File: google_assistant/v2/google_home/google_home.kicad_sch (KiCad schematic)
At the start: 22 parts, among them J1 Conn_01x16_MountingPin, J2 AudioJack2_SwitchT, J3 Conn_02x05_Odd_Even, J4 Conn_01x02, SW1 SW_SPDT, SW2 SW_SPDT, U1 R-78E5.0-1.0

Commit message: Fixed FFC connector footprint
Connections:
- net +5V: now also J1.2 (Pin_2), J1.3 (Pin_3), J1.4 (Pin_4), J1.5 (Pin_5), J1.6 (Pin_6), J1.7 (Pin_7); no longer J1.10 (Pin_10), J1.11 (Pin_11), J1.12 (Pin_12), J1.13 (Pin_13), J1.14 (Pin_14), J1.15 (Pin_15)
- net GND: now also J1.11 (Pin_11), J1.12 (Pin_12), J1.13 (Pin_13), J1.14 (Pin_14), J1.15 (Pin_15), J1.8 (Pin_8); no longer J1.2 (Pin_2), J1.3 (Pin_3), J1.4 (Pin_4), J1.5 (Pin_5), J1.6 (Pin_6), J1.9 (Pin_9)
- net at SW1.2 (B): now also J1.16 (Pin_16); no longer J1.1 (Pin_1)
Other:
- moved on the sheet: J1
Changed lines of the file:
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@@
+    (stroke (width 0) (type default))
+  )
+  (wire (pts (xy 190.5 48.26) (xy 195.58 48.26))
     (stroke (width 0) (type default))
   )
@@
     )
   )
-  (symbol (lib_id "power:GND") (at 190.5 96.52 0) (unit 1)
-    (in_bom yes) (on_board yes) (dnp no) (fields_autoplaced)
-    (property "Reference" "#PWR01" (at 190.5 102.87 0)
-      (effects (font (size 1.27 1.27)) hide)
-    )
-    (property "Value" "GND" (at 190.5 101.6 0)
-      (effects (font (size 1.27 1.27)))
-    )
-    (property "Footprint" "" (at 190.5 96.52 0)
-      (effects (font (size 1.27 1.27)) hide)
-    )
-    (property "Datasheet" "" (at 190.5 96.52 0)
+  (symbol (lib_id "power:GND") (at 195.58 48.26 0) (unit 1)
+    (in_bom yes) (on_board yes) (dnp no) (fields_autoplaced)
+    (property "Reference" "#PWR01" (at 195.58 54.61 0)
+      (effects (font (size 1.27 1.27)) hide)
+    )
+    (property "Value" "GND" (at 195.58 53.34 0)
+      (effects (font (size 1.27 1.27)))
+    )
+    (property "Footprint" "" (at 195.58 48.26 0)
+      (effects (font (size 1.27 1.27)) hide)
+    )
+    (property "Datasheet" "" (at 195.58 48.26 0)
       (effects (font (size 1.27 1.27)) hide)
     )
@@
     )
   )
-  (symbol (lib_id "Connector_Generic_MountingPin:Conn_01x16_MountingPin") (at 190.5 71.12 0) (unit 1)
-    (in_bom yes) (on_board yes) (dnp no) (fields_autoplaced)
-    (property "Reference" "J1" (at 193.04 71.4756 0)
+  (symbol (lib_id "Connector_Generic_MountingPin:Conn_01x16_MountingPin") (at 190.5 73.66 0) (mirror x) (unit 1)
+    (in_bom yes) (on_board yes) (dnp no)
+    (property "Reference" "J1" (at 193.04 73.3044 0)
       (effects (font (size 1.27 1.27)) (justify left))
     )
-    (property "Value" "Conn_01x16_MountingPin" (at 193.04 74.0156 0)
+    (property "Value" "Conn_01x16_MountingPin" (at 193.04 70.7644 0)
       (effects (font (size 1.27 1.27)) (justify left))
     )
-    (property "Footprint" "Connector_FFC-FPC:TE_1-1734839-6_1x16-1MP_P0.5mm_Horizontal" (at 190.5 71.12 0)
-      (effects (font (size 1.27 1.27)) hide)
-    )
-    (property "Datasheet" "~" (at 190.5 71.12 0)
-      (effects (font (size 1.27 1.27)) hide)
-    )
+    (property "Footprint" "Connector_FFC-FPC:TE_1-1734839-6_1x16-1MP_P0.5mm_Horizontal" (at 190.5 73.66 0)
+      (effects (font (size 1.27 1.27)) hide)
+    )
+    (property "Datasheet" "~" (at 190.5 73.66 0)
+      (effects (font (size 1.27 1.27)) hide)
+    )

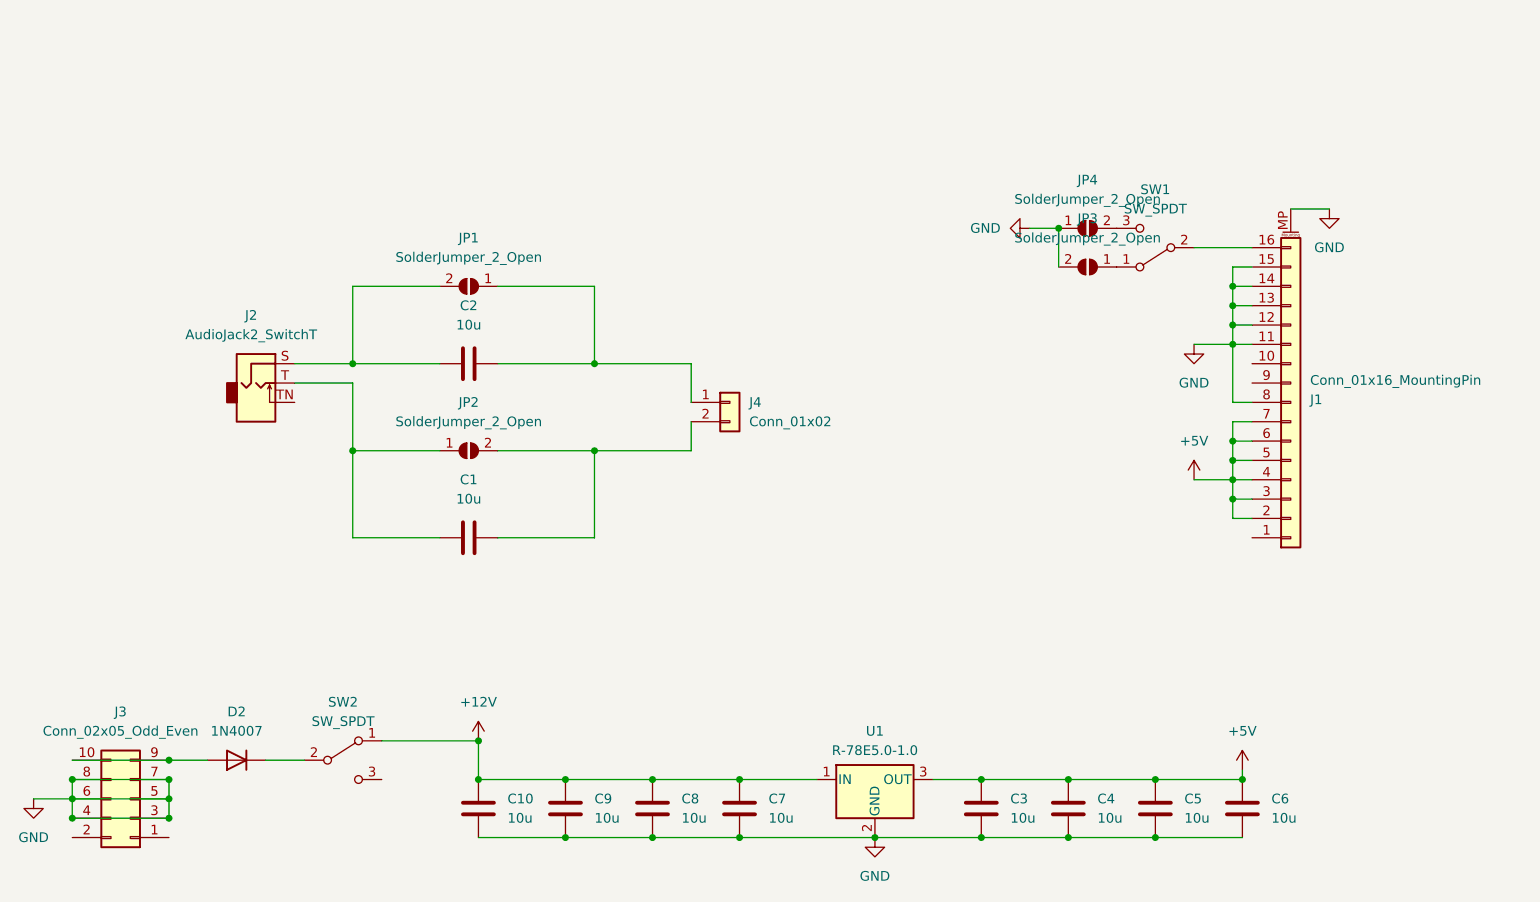
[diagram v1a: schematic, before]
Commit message: Added transformer
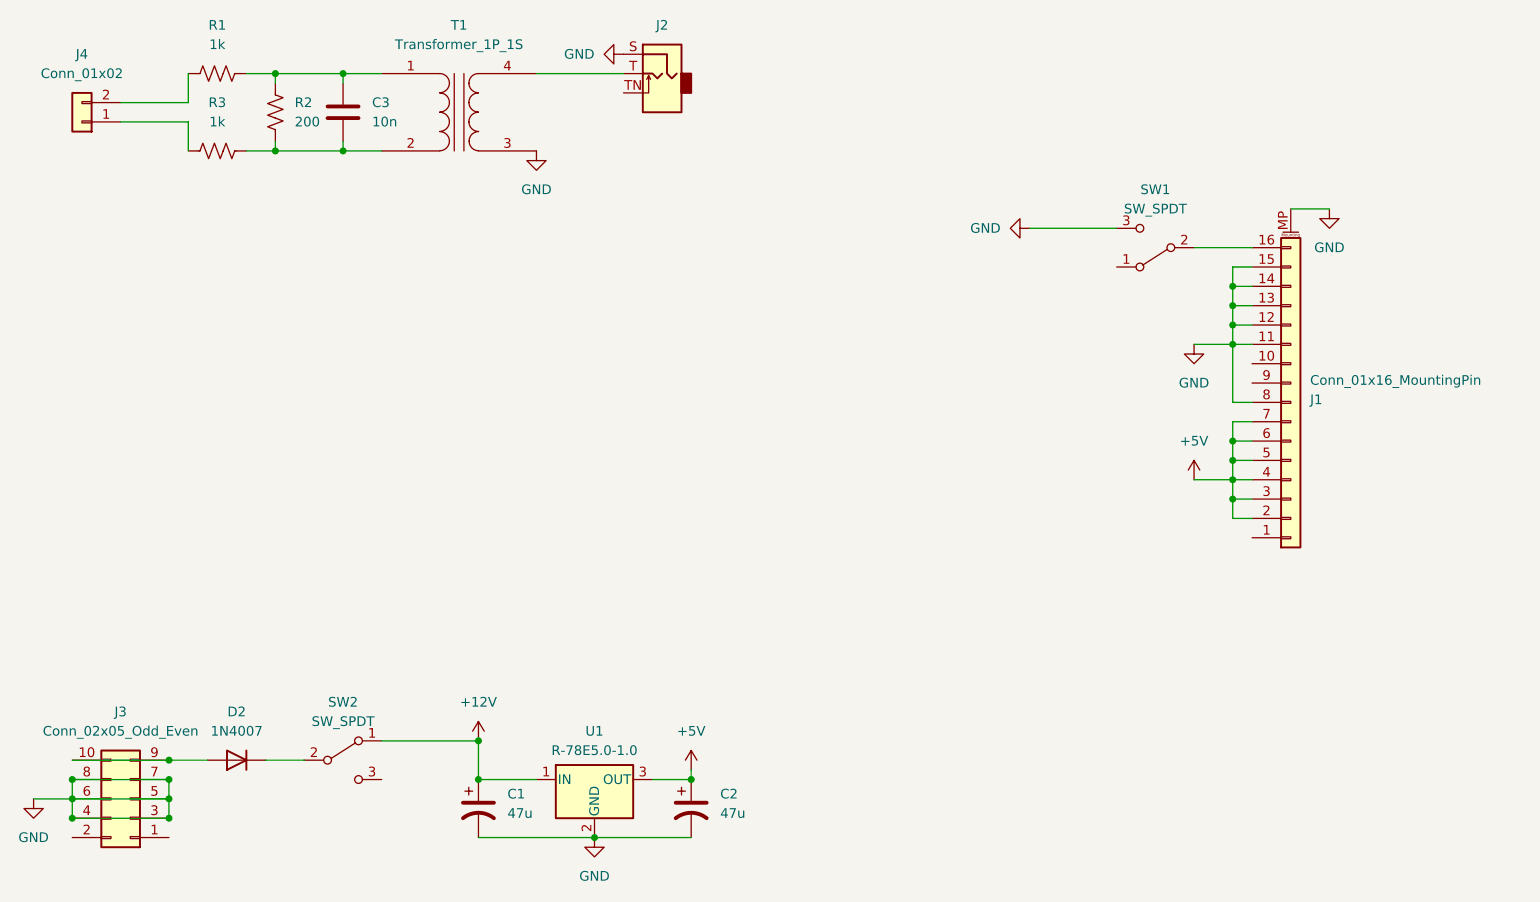
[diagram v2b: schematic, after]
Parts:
- removed C1, C10, C2, C4, C5, C6, C7, C8, C9: 10u, Capacitor_SMD:C_0805_2012Metric, symbol Device:C
- removed JP1, JP2, JP3, JP4: SolderJumper_2_Open, Jumper:SolderJumper-2_P1.3mm_Open_RoundedPad1.0x1.5mm, symbol Jumper:SolderJumper_2_Open
- added C1, C2: 47u, Capacitor_THT:CP_Radial_D6.3mm_P2.50mm, symbol Device:C_Polarized_US
- added R1, R3: 1k, Resistor_SMD:R_0603_1608Metric, symbol Device:R_US
- added R2: 200, Resistor_SMD:R_0603_1608Metric, symbol Device:R_US
- added T1: Transformer_1P_1S, AlexCustom:EI14, symbol Device:Transformer_1P_1S
- C3: value 10u -> 10n; footprint Capacitor_SMD:C_0805_2012Metric -> Capacitor_SMD:C_0603_1608Metric
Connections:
- net +12V: now also C1.1
- net +5V: now also C2.1; no longer C3.2
- net GND: now also J2.S, SW1.3 (C), C1.2, C2.2, T1.3 (SA); no longer C3.1
- net at J4.1 (Pin_1): now also R3.2
- net at J2.T: now also T1.4 (SB)
- net at J4.2 (Pin_2): now also R1.2
- new net: C3.2, R2.2, R3.1, T1.2 (AB)
- new net: C3.1, R1.1, R2.1, T1.1 (AA)
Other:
- moved on the sheet: J2, J4, U1

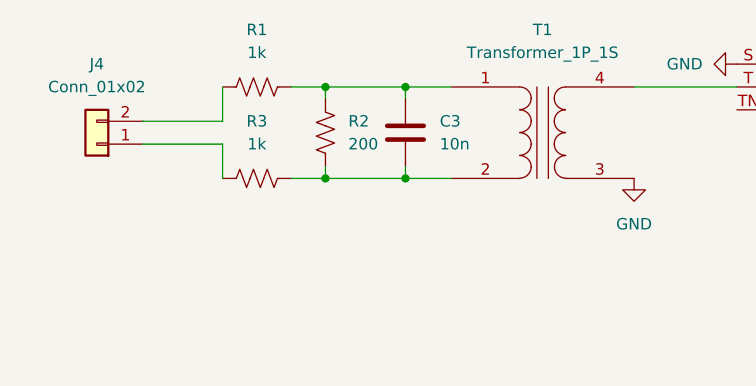
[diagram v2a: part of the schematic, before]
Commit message: Simplified schematic
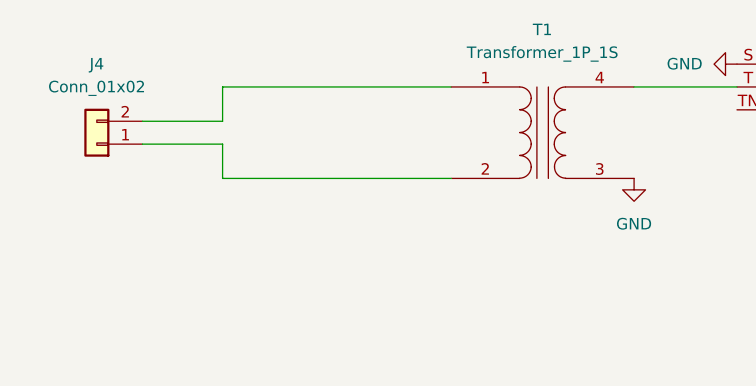
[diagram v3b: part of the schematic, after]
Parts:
- removed C3: 10n, Capacitor_SMD:C_0603_1608Metric, symbol Device:C
- removed R1, R3: 1k, Resistor_SMD:R_0603_1608Metric, symbol Device:R_US
- removed R2: 200, Resistor_SMD:R_0603_1608Metric, symbol Device:R_US
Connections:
- net at T1.2 (AB): now also J4.1 (Pin_1)
- net at T1.1 (AA): now also J4.2 (Pin_2)
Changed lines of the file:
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@@
   (junction (at 83.82 123.19) (diameter 0) (color 0 0 0 0)
   )
-  (junction (at 57.15 40.64) (diameter 0) (color 0 0 0 0)
-  )
   (junction (at 182.88 58.42) (diameter 0) (color 0 0 0 0)
   )
   (junction (at 43.18 128.27) (diameter 0) (color 0 0 0 0)
   )
-  (junction (at 66.04 30.48) (diameter 0) (color 0 0 0 0)
-  )
   (junction (at 182.88 63.5) (diameter 0) (color 0 0 0 0)
   )
@@
   (junction (at 30.48 128.27) (diameter 0) (color 0 0 0 0)
   )
-  (junction (at 66.04 40.64) (diameter 0) (color 0 0 0 0)
-  )
   (junction (at 43.18 125.73) (diameter 0) (color 0 0 0 0)
   )
   (junction (at 83.82 118.11) (diameter 0) (color 0 0 0 0)
   )
-  (junction (at 57.15 30.48) (diameter 0) (color 0 0 0 0)
-  )
   (junction (at 182.88 83.82) (diameter 0) (color 0 0 0 0)
   )
-  (wire (pts (xy 57.15 40.64) (xy 66.04 40.64))
-    (stroke (width 0) (type default))
-  )
   (wire (pts (xy 182.88 81.28) (xy 182.88 78.74))
     (stroke (width 0) (type default))
   )
-  (wire (pts (xy 53.34 30.48) (xy 57.15 30.48))
-    (stroke (width 0) (type default))
-  )
   (wire (pts (xy 30.48 123.19) (xy 43.18 123.19))
     (stroke (width 0) (type default))
   )
+  (wire (pts (xy 45.72 40.64) (xy 71.12 40.64))
+    (stroke (width 0) (type default))
+  )
   (wire (pts (xy 45.72 36.83) (xy 45.72 40.64))
     (stroke (width 0) (type default))
@@
     (stroke (width 0) (type default))
   )
-  (wire (pts (xy 66.04 30.48) (xy 66.04 31.75))
-    (stroke (width 0) (type default))
-  )
   (wire (pts (xy 182.88 76.2) (xy 185.42 76.2))
     (stroke (width 0) (type default))
@@
     (stroke (width 0) (type default))
   )
-  (wire (pts (xy 57.15 39.37) (xy 57.15 40.64))
-    (stroke (width 0) (type default))
-  )
   (wire (pts (xy 182.88 58.42) (xy 182.88 60.96))
     (stroke (width 0) (type default))
@@
     (stroke (width 0) (type default))
   )
-  (wire (pts (xy 57.15 30.48) (xy 57.15 31.75))
-    (stroke (width 0) (type default))
-  )
-  (wire (pts (xy 53.34 40.64) (xy 57.15 40.64))
-    (stroke (width 0) (type default))
-  )
   (wire (pts (xy 177.8 53.34) (xy 185.42 53.34))
     (stroke (width 0) (type default))
@@
     (stroke (width 0) (type default))
   )
-  (wire (pts (xy 66.04 30.48) (xy 71.12 30.48))
-    (stroke (width 0) (type default))
-  )
   (wire (pts (xy 43.18 123.19) (xy 43.18 125.73))
     (stroke (width 0) (type default))
@@
     (stroke (width 0) (type default))
   )
-  (wire (pts (xy 66.04 40.64) (xy 71.12 40.64))
-    (stroke (width 0) (type default))
-  )
   (wire (pts (xy 83.82 123.19) (xy 91.44 123.19))
     (stroke (width 0) (type default))
@@
     (stroke (width 0) (type default))
   )
+  (wire (pts (xy 45.72 30.48) (xy 71.12 30.48))
+    (stroke (width 0) (type default))
+  )
   (wire (pts (xy 182.88 60.96) (xy 185.42 60.96))
     (stroke (width 0) (type default))
@@
     (stroke (width 0) (type default))
   )
-  (wire (pts (xy 57.15 30.48) (xy 66.04 30.48))
-    (stroke (width 0) (type default))
-  )
   (wire (pts (xy 30.48 125.73) (xy 43.18 125.73))
     (stroke (width 0) (type default))
@@
   )
   (wire (pts (xy 185.42 73.66) (xy 182.88 73.66))
-    (stroke (width 0) (type default))
-  )
-  (wire (pts (xy 66.04 39.37) (xy 66.04 40.64))
     (stroke (width 0) (type default))
   )
@@
         (path "/02c9e3d6-9669-4f4c-9380-0c978d4a8549"
           (reference "#PWR08") (unit 1)
-        )
-      )
-    )
-  )
-  (symbol (lib_id "Device:R_US") (at 49.53 40.64 270) (unit 1)
-    (in_bom yes) (on_board yes) (dnp no) (fields_autoplaced)
-    (property "Reference" "R3" (at 49.53 34.29 90)
-      (effects (font (size 1.27 1.27)))
-    )
-    (property "Value" "1k" (at 49.53 36.83 90)
-      (effects (font (size 1.27 1.27)))
-    )
-    (property "Footprint" "Resistor_SMD:R_0603_1608Metric" (at 49.276 41.656 90)
-      (effects (font (size 1.27 1.27)) hide)
-    )
-    (property "Datasheet" "~" (at 49.53 40.64 0)
-      (effects (font (size 1.27 1.27)) hide)
-    )
-    (pin "2")
-    (pin "1")
-    (instances
-      (project "google_home"
-        (path "/02c9e3d6-9669-4f4c-9380-0c978d4a8549"
-          (reference "R3") (unit 1)
         )
       )
@@
         (path "/02c9e3d6-9669-4f4c-9380-0c978d4a8549"
           (reference "#PWR01") (unit 1)
-        )
-      )
-    )
-  )
-  (symbol (lib_id "Device:C") (at 66.04 35.56 0) (unit 1)
-    (in_bom yes) (on_board yes) (dnp no) (fields_autoplaced)
-    (property "Reference" "C3" (at 69.85 34.29 0)
-      (effects (font (size 1.27 1.27)) (justify left))
-    )
-    (property "Value" "10n" (at 69.85 36.83 0)
-      (effects (font (size 1.27 1.27)) (justify left))
-    )
-    (property "Footprint" "Capacitor_SMD:C_0603_1608Metric" (at 67.0052 39.37 0)
-      (effects (font (size 1.27 1.27)) hide)
-    )
-    (property "Datasheet" "~" (at 66.04 35.56 0)
-      (effects (font (size 1.27 1.27)) hide)
-    )
-    (pin "1")
-    (pin "2")
-    (instances
-      (project "google_home"
-        (path "/02c9e3d6-9669-4f4c-9380-0c978d4a8549"
-          (reference "C3") (unit 1)
         )
       )
@@
     )
   )
-  (symbol (lib_id "Device:R_US") (at 49.53 30.48 270) (unit 1)
-    (in_bom yes) (on_board yes) (dnp no) (fields_autoplaced)
-    (property "Reference" "R1" (at 49.53 24.13 90)
-      (effects (font (size 1.27 1.27)))
-    )
-    (property "Value" "1k" (at 49.53 26.67 90)
-      (effects (font (size 1.27 1.27)))
-    )
-    (property "Footprint" "Resistor_SMD:R_0603_1608Metric" (at 49.276 31.496 90)
-      (effects (font (size 1.27 1.27)) hide)
-    )
-    (property "Datasheet" "~" (at 49.53 30.48 0)
-      (effects (font (size 1.27 1.27)) hide)
-    )
-    (pin "2")
-    (pin "1")
-    (instances
-      (project "google_home"
-        (path "/02c9e3d6-9669-4f4c-9380-0c978d4a8549"
-          (reference "R1") (unit 1)
-        )
-      )
-    )
-  )
   (symbol (lib_id "power:GND") (at 177.8 66.04 0) (unit 1)
     (in_bom yes) (on_board yes) (dnp no) (fields_autoplaced)
@@
         )
       )
-    )
-  )
-  (symbol (lib_id "Device:R_US") (at 57.15 35.56 0) (unit 1)
-    (in_bom yes) (on_board yes) (dnp no) (fields_autoplaced)
-    (property "Reference" "R2" (at 59.69 34.29 0)
-      (effects (font (size 1.27 1.27)) (justify left))
-    )
-    (property "Value" "200" (at 59.69 36.83 0)
-      (effects (font (size 1.27 1.27)) (justify left))
-    )
-    (property "Footprint" "Resistor_SMD:R_0603_1608Metric" (at 58.166 35.814 90)
-      (effects (font (size 1.27 1.27)) hide)
-    )
-    (property "Datasheet" "~" (at 57.15 35.56 0)
-      (effects (font (size 1.27 1.27)) hide)
-    )
-    (pin "2")
-    (pin "1")
-    (instances
-      (project "google_home"
-        (path "/02c9e3d6-9669-4f4c-9380-0c978d4a8549"
-          (reference "R2") (unit 1)
-        )
-      )

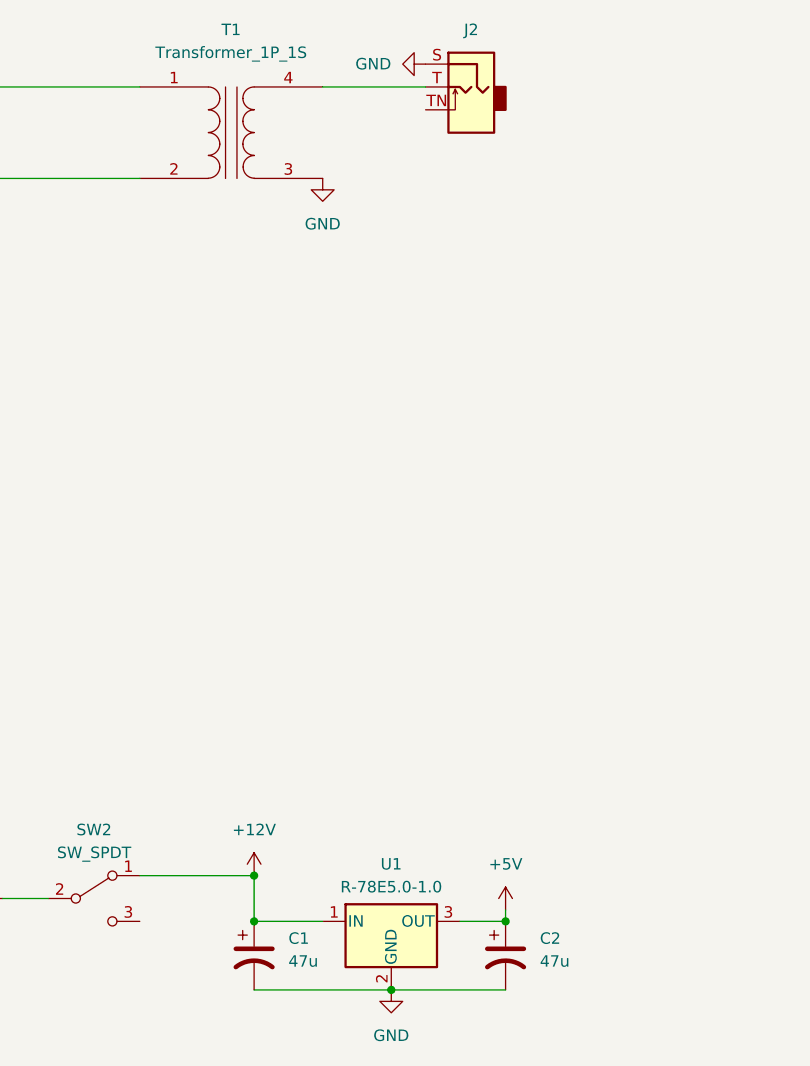
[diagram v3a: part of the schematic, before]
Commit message: Updated trace widths and capacitor values
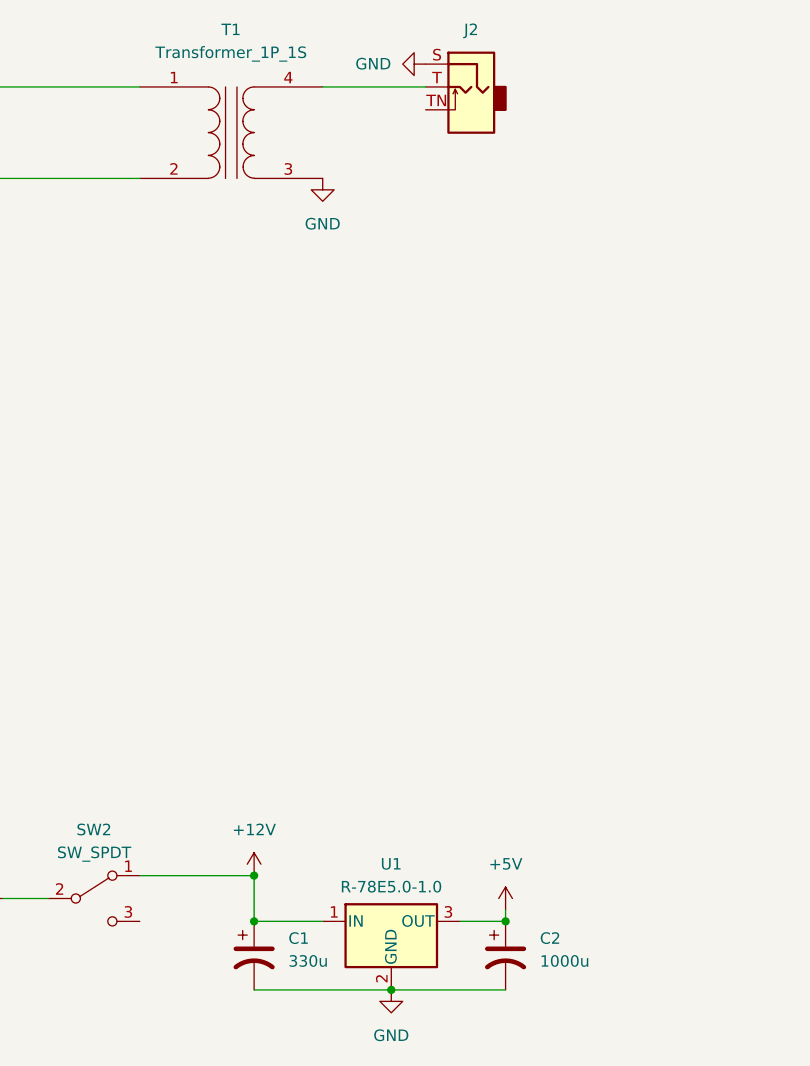
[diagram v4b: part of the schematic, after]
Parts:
- C1: value 47u -> 330u; footprint Capacitor_THT:CP_Radial_D6.3mm_P2.50mm -> Capacitor_THT:CP_Radial_D8.0mm_P5.00mm
- C2: value 47u -> 1000u; footprint Capacitor_THT:CP_Radial_D6.3mm_P2.50mm -> Capacitor_THT:CP_Radial_D8.0mm_P5.00mm
